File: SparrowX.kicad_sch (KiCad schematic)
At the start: 30 parts, among them J1 NORTH, J2 SOUTH, J3 WEST, J4 EAST, U1 LMR43610MSC3RPERQ1, U2 LD49100PU33RY, U3 STM32G0B1CBU6, U4 TCAN332G, U5 TCAN332G

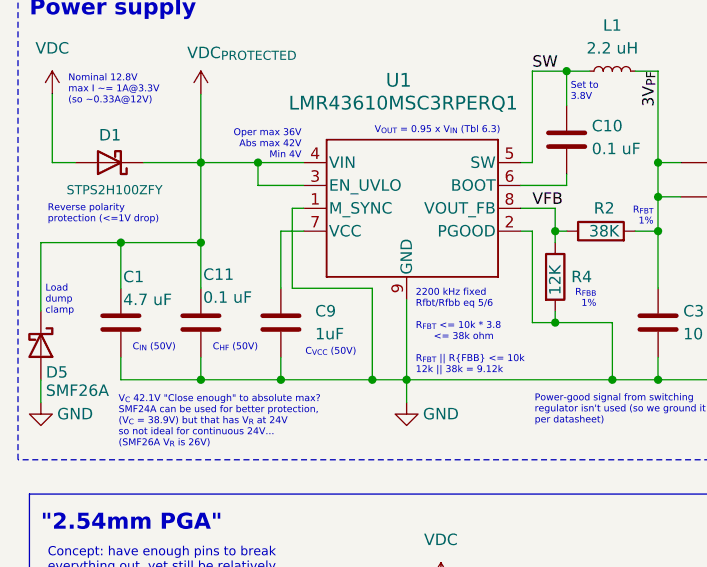
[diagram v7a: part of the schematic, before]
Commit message: C9 doesn't have to be 50V
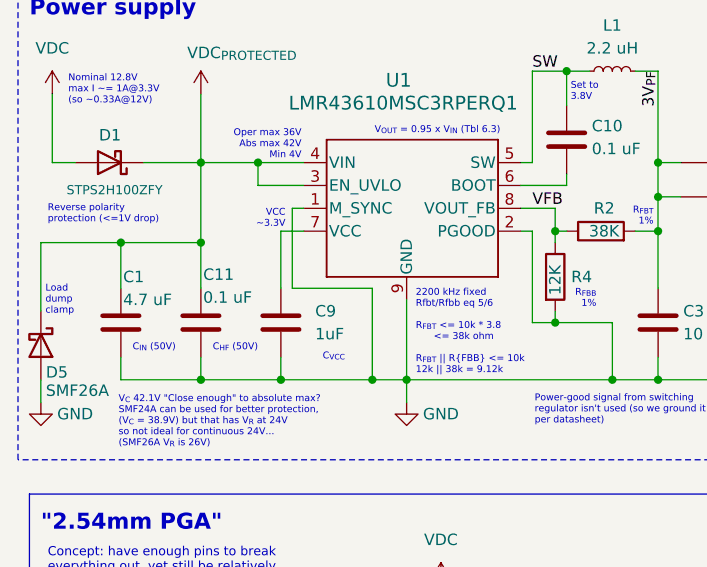
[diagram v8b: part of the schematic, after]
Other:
- note added: "C_{VCC}"
- note added: "VCC ~3.3V"
- note removed: "C_{VCC} (50V)"
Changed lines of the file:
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@@
+		)
+	)
+	(text "VCC\n~3.3V"
+		(exclude_from_sim no)
+		(at 42.418 40.386 0)
+		(effects
+			(font
+				(size 0.762 0.762)
+			)
+			(justify right bottom)
 		)
 	)
@@
 		)
 	)
-	(text "C_{VCC} (50V)"
-		(exclude_from_sim no)
-		(at 50.292 54.61 0)
-		(effects
-			(font
+	(text "C_{VCC}"
+		(exclude_from_sim no)
+		(at 49.022 55.118 0)
+		(effects
+			(font
